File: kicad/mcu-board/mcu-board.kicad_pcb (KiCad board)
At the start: 2 copper layers, 54.5 x 46.3 mm, 64 parts, among them J10 Conn_01x02, J11 Conn_01x02, J12 UJ20-C-H-G-SMT-P16-TR, J13 Conn_01x06, J2 Conn_01x06, J3 Conn_01x01, J4 Conn_01x02, J5 Conn_01x02, J6 Conn_01x02, J7 Conn_01x03, J8 Conn_01x04, J9 Conn_01x02, Q1 Q_NPN_CEB, SW1 SW_Push, SW2 SW_Push, U1 Lora1276-C1-868, U2 ESP32-S3-WROOM-1U-N16R8, U3 LM66200DRLR, U4 AP3445LW6-7

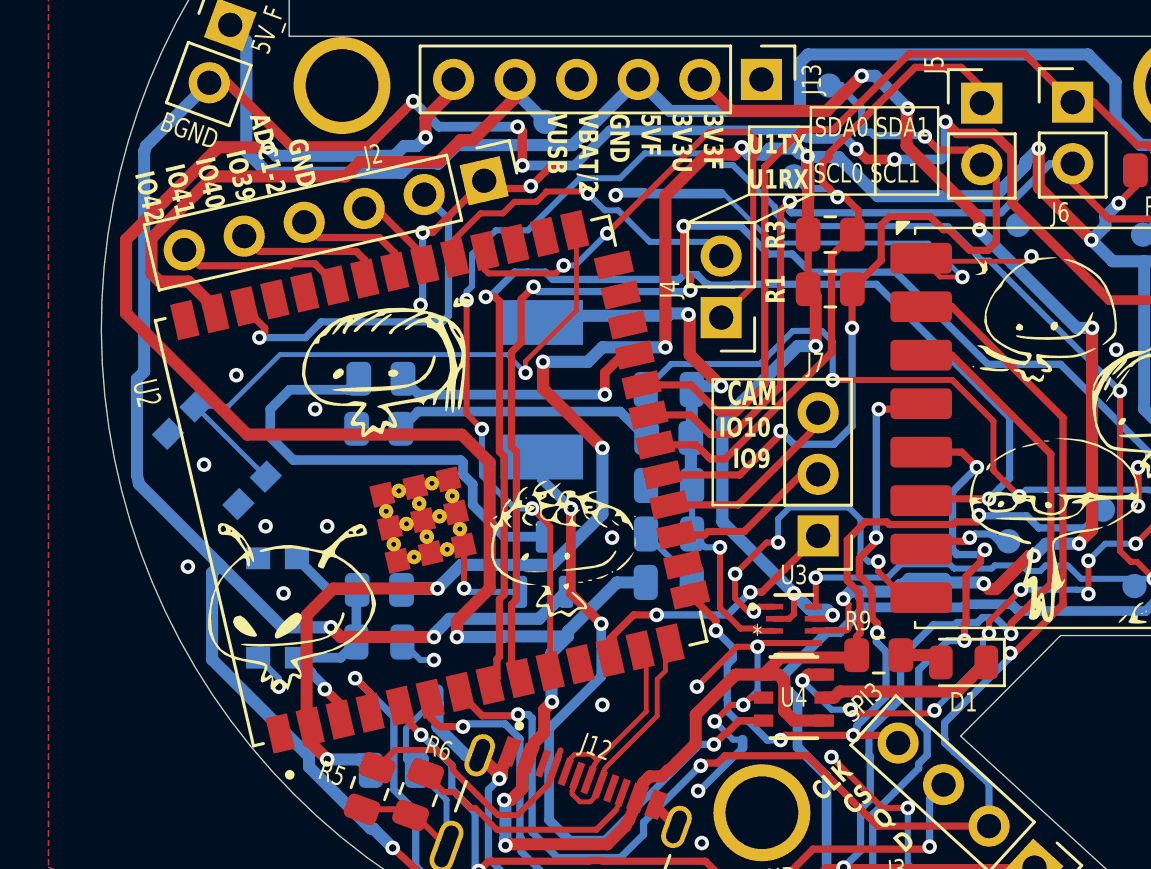
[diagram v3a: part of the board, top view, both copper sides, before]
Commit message: chore: Fixed led footprint from 0805 to 0603, and edited title for buzzer
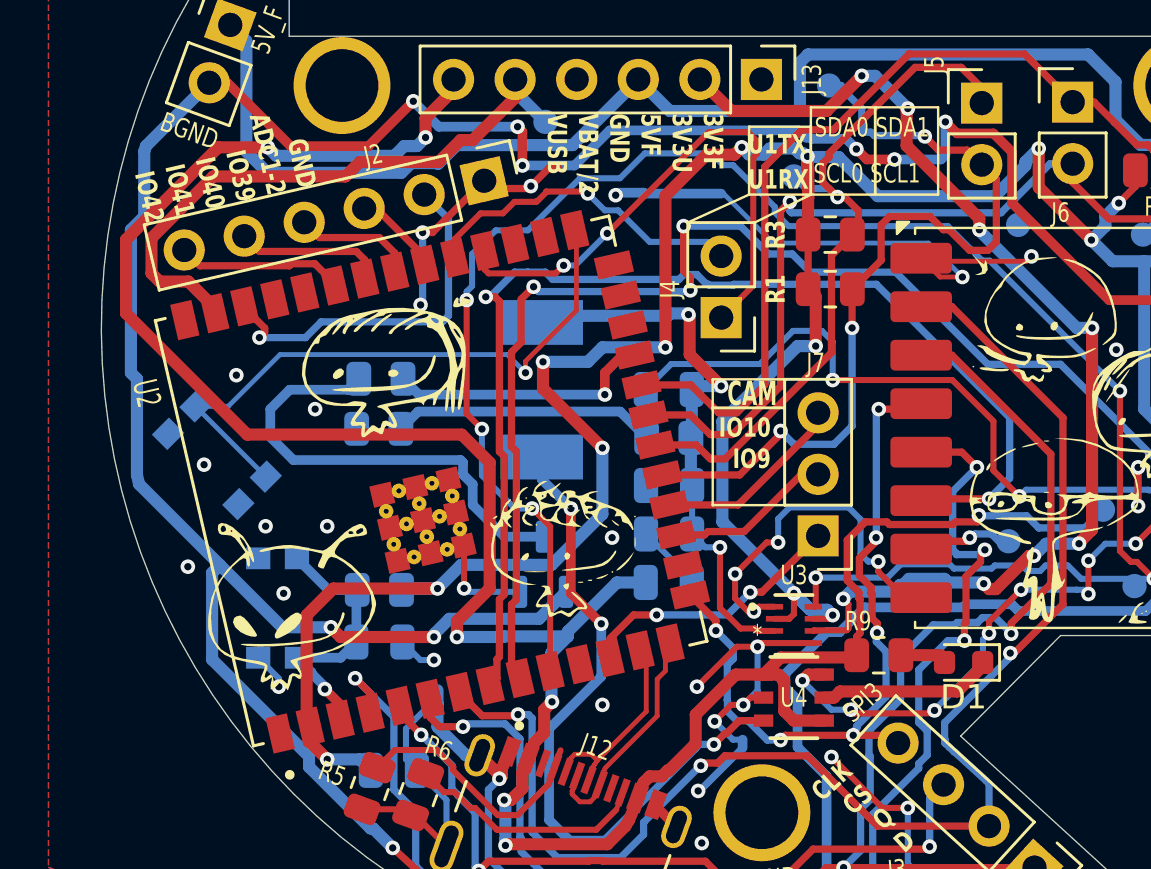
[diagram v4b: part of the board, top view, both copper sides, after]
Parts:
- D1: footprint LED_SMD:LED_0805_2012Metric -> LED_SMD:LED_0603_1608Metric
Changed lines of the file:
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@@
 		(embedded_fonts no)
 	)
-	(footprint "LED_SMD:LED_0805_2012Metric"
+	(footprint "LED_SMD:LED_0603_1608Metric"
 		(layer "F.Cu")
 		(at 113 112.3 180)
-		(descr "LED SMD 0805 (2012 Metric), square (rectangular) end terminal, IPC-7351 nominal, (Body size source: https://docs.google.com/spreadsheets/d/1BsfQQcO9C6DZCsRaXUlFlo91Tg2WpOkGARC1WS5S8t0/edit?usp=sharing), generated with kicad-footprint-generator")
+		(descr "LED SMD 0603 (1608 Metric), square (rectangular) end terminal, IPC-7351 nominal, (Body size source: http://www.tortai-tech.com/upload/download/2011102023233369053.pdf), generated with kicad-footprint-generator")
 		(tags "LED")
 		(property "Reference" "D1"
-			(at 0 -1.65 0)
+			(at 0 -1.43 180)
 			(layer "F.SilkS")
 			(effects
 				(font
-					(size 0.8 0.6)
+					(size 1 1)
 					(thickness 0.15)
 				)
@@
 		)
 		(property "Value" "LED"
-			(at 0 1.65 0)
+			(at 0 1.43 180)
 			(layer "F.Fab")
 			(effects
@@
 		)
 		(property "Datasheet" "~"
-			(at 0 0 0)
+			(at 0 0 180)
 			(layer "F.Fab")
 			(hide yes)
@@
 		)
 		(property "Description" "Light emitting diode"
-			(at 0 0 0)
+			(at 0 0 180)
 			(layer "F.Fab")
 			(hide yes)
@@
 		(attr smd)
 		(fp_line
-			(start 1 -0.96)
-			(end -1.685 -0.96)
+			(start 0.8 -0.735)
+			(end -1.485 -0.735)
 			(stroke
 				(width 0.12)
@@
 		)
 		(fp_line
-			(start -1.685 0.96)
-			(end 1 0.96)
+			(start -1.485 0.735)
+			(end 0.8 0.735)
 			(stroke
 				(width 0.12)
@@
 		)
 		(fp_line
-			(start -1.685 -0.96)
-			(end -1.685 0.96)
+			(start -1.485 -0.735)
+			(end -1.485 0.735)
 			(stroke
 				(width 0.12)
@@
 		)
 		(fp_line
-			(start 1.68 0.95)
-			(end -1.68 0.95)
+			(start 1.48 0.73)
+			(end -1.48 0.73)
 			(stroke
 				(width 0.05)
@@
 		)
 		(fp_line
-			(start 1.68 -0.95)
-			(end 1.68 0.95)
+			(start 1.48 -0.73)
+			(end 1.48 0.73)
 			(stroke
 				(width 0.05)
@@
 		)
 		(fp_line
-			(start -1.68 0.95)
-			(end -1.68 -0.95)
+			(start -1.48 0.73)
+			(end -1.48 -0.73)
 			(stroke
 				(width 0.05)
@@
 		)
 		(fp_line
-			(start -1.68 -0.95)
-			(end 1.68 -0.95)
+			(start -1.48 -0.73)
+			(end 1.48 -0.73)
 			(stroke
 				(width 0.05)
@@
 		)
 		(fp_line
-			(start 1 0.6)
-			(end 1 -0.6)
+			(start 0.8 0.4)
+			(end 0.8 -0.4)
 			(stroke
 				(width 0.1)
@@
 		)
 		(fp_line
-			(start 1 -0.6)
-			(end -0.7 -0.6)
+			(start 0.8 -0.4)
+			(end -0.5 -0.4)
 			(stroke
 				(width 0.1)
@@
 		)
 		(fp_line
-			(start -0.7 -0.6)
-			(end -1 -0.3)
+			(start -0.5 -0.4)
+			(end -0.8 -0.1)
 			(stroke
 				(width 0.1)
@@
 		)
 		(fp_line
-			(start -1 0.6)
-			(end 1 0.6)
+			(start -0.8 0.4)
+			(end 0.8 0.4)
 			(stroke
 				(width 0.1)
@@
 		)
 		(fp_line
-			(start -1 -0.3)
-			(end -1 0.6)
+			(start -0.8 -0.1)
+			(end -0.8 0.4)
 			(stroke
 				(width 0.1)
@@
 		)
 		(fp_text user "${REFERENCE}"
-			(at 0 0 0)
+			(at 0 0 180)
 			(layer "F.Fab")
 			(effects
 				(font
-					(size 0.5 0.5)
-					(thickness 0.08)
+					(size 0.4 0.4)
+					(thickness 0.06)
 				)
 			)
 		)
 		(pad "1" smd roundrect
-			(at -0.9375 0 180)
-			(size 0.975 1.4)
+			(at -0.7875 0 180)
+			(size 0.875 0.95)
 			(layers "F.Cu" "F.Mask" "F.Paste")
 			(roundrect_rratio 0.25)
@@
 		)
 		(pad "2" smd roundrect
-			(at 0.9375 0 180)
-			(size 0.975 1.4)
+			(at 0.7875 0 180)
+			(size 0.875 0.95)
 			(layers "F.Cu" "F.Mask" "F.Paste")
 			(roundrect_rratio 0.25)
@@
 		)
 		(embedded_fonts no)
-		(model "${KICAD9_3DMODEL_DIR}/LED_SMD.3dshapes/LED_0805_2012Metric.stpZ"
+		(model "${KICAD9_3DMODEL_DIR}/LED_SMD.3dshapes/LED_0603_1608Metric.stpZ"
 			(offset
 				(xyz 0 0 0)
@@
 	)
 	(segment
-		(start 78.9 100.600599)
-		(end 79.2 100.300599)
-		(width 0.5)
-		(layer "B.Cu")
-		(net 57)
-	)
-	(segment
 		(start 88.65 119.15)
 		(end 89.45 119.95)
@@
 	)
 	(segment
+		(start 78.9 100.600599)
+		(end 78.65 100.350599)
+		(width 0.5)
+		(layer "B.Cu")
+		(net 57)
+	)
+	(segment
 		(start 85.999 116.611075)
 		(end 88.537925 119.15)
@@
 	)
 	(segment
-		(start 78.986115 104.944365)
-		(end 78.9 104.568454)
-		(width 0.5)
-		(layer "B.Cu")
-		(net 57)
-	)
-	(segment
-		(start 82.320875 108.279125)
-		(end 78.986115 104.944365)
-		(width 0.5)
-		(layer "B.Cu")
-		(net 57)
-	)
-	(segment
 		(start 123.991364 97.35)
 		(end 121.7 97.35)
@@
 	)
 	(segment
-		(start 79.2 91.222341)
-		(end 79.273606 90.994482)
+		(start 95.4875 110.5)
+		(end 91.787925 110.5)
 		(width 0.5)
 		(layer "B.Cu")
@@
 	)
 	(segment
-		(start 95.4875 110.5)
-		(end 91.787925 110.5)
+		(start 79.2 93.9)
+		(end 79.2 91.222341)
 		(width 0.5)
 		(layer "B.Cu")
@@
 	)
 	(segment
-		(start 84.89175 110.85)
-		(end 82.320875 108.279125)
+		(start 78.9 104.568454)
+		(end 78.9 100.600599)
 		(width 0.5)
 		(layer "B.Cu")
@@
 	)
 	(segment
-		(start 91.787925 110.5)
-		(end 91.15 111.137925)
+		(start 78.986115 104.944365)
+		(end 78.9 104.568454)
 		(width 0.5)
 		(layer "B.Cu")
@@
 	)
 	(segment
-		(start 78.9 104.568454)
-		(end 78.9 100.600599)
+		(start 84.89175 110.85)
+		(end 82.320875 108.279125)
 		(width 0.5)
 		(layer "B.Cu")
@@
 	)
 	(segment
-		(start 79.2 100.300599)
-		(end 79.2 91.222341)
+		(start 91.787925 110.5)
+		(end 91.15 111.137925)
+		(width 0.5)
+		(layer "B.Cu")
+		(net 57)
+	)
+	(segment
+		(start 79.2 91.222341)
+		(end 79.273606 90.994482)
 		(width 0.5)
 		(layer "B.Cu")
@@
 	)
 	(segment
+		(start 78.65 94.45)
+		(end 79.2 93.9)
+		(width 0.5)
+		(layer "B.Cu")
+		(net 57)
+	)
+	(segment
+		(start 82.320875 108.279125)
+		(end 78.986115 104.944365)
+		(width 0.5)
+		(layer "B.Cu")
+		(net 57)
+	)
+	(segment
 		(start 86.9 110.85)
 		(end 84.89175 110.85)
@@
 	)
 	(segment
-		(start 106.663571 90.648)
-		(end 106.498 90.648)
-		(width 0.4)
+		(start 78.65 100.350599)
+		(end 78.65 94.45)
+		(width 0.5)
 		(layer "B.Cu")
 		(net 57)
@@
 		(layer "B.Cu")
 		(net 57)
+	)
+	(segment
+		(start 106.663571 90.648)
+		(end 106.498 90.648)
+		(width 0.4)
+		(layer "B.Cu")
+		(net 57)

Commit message: fix: Fixed the mcu-board and preparing for the panelisation
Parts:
- added R12: 5.1k, Resistor_SMD:R_0805_2012Metric, B.Cu at (125.1, 103.5)
- moved TP5 15.9 mm to (130.1, 95.3)
- moved TP4 9.68 mm to (124.8, 98.1)
- moved TP6 8.49 mm to (129.5, 105.7)
- moved TP7 7.71 mm to (129.7, 103.5)
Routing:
- net /LoRa_IRQ: track 56.8 -> 63.9 mm
- net /POWER_ST: track 76.2 -> 82.1 mm
- net +3V3: track 124.4 -> 130.0 mm
- net /DI1: track 3.32 -> 4.54 mm
- net /DI2: track 4.61 -> 5.28 mm
- net GND: vias 45 -> 44
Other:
- board text added: "DI1"
- board text added: "DI2"
- board text added: "DI4 DI3"
- board text removed: "DI1 DI2"
- board text removed: "DI3 DI4"

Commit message: feat: finished pcb, might add more artwork later?
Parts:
- removed the C6 at (100.8, 109.0)
- removed D1: LED, LED_SMD:LED_0603_1608Metric
- removed the G*** at (83.6, 109.0)
- removed the G*** at (121.7, 101.8)
- removed the G*** at (89.4, 100.2)
- removed the G*** at (116.5, 106.5)
- removed the G*** at (96.7, 107.5)
- removed the G*** at (116.5, 98.2)
- removed J10, J11, J9: Conn_01x02, Connector_PinHeader_2.54mm:PinHeader_1x02_P2.54mm_Vertical
- removed J13: Conn_01x06, Connector_PinHeader_2.54mm:PinHeader_1x06_P2.54mm_Vertical
- removed the J6 at (117.5, 89.2)
- removed J8: Conn_01x04, Connector_PinHeader_2.54mm:PinHeader_1x04_P2.54mm_Vertical
- removed L1: 2u2H, PSAT_Library:IND_SPM6530T-1R5M100
- removed the R7 at (100.8, 103.0)
- removed the R8 at (88.9, 102.7)
- removed the R9 at (109.5, 112.0)
- removed the TP15 at (120.4, 94.7)
- added C7: 0.1uf, Capacitor_SMD:C_0805_2012Metric, B.Cu at (84.9, 110.7)
- added C8: 1u, Capacitor_SMD:C_0805_2012Metric, B.Cu at (123.4, 100.1)
- added C9: 1u, Capacitor_SMD:C_0805_2012Metric, B.Cu at (123.4, 102.1)
- added G***: LOGO, LOGO, F.Cu at (95.8, 121.3)
- added G***: LOGO, LOGO, B.Cu at (112.0, 94.2)
- added G***: LOGO, LOGO, F.Cu at (119.2, 102.5)
- added G***: LOGO, LOGO, F.Cu at (113.5, 88.4)
- added G***: LOGO, LOGO, F.Cu at (91.5, 104.8)
- added G***: LOGO, LOGO, B.Cu at (117.0, 89.5)
- added G***: LOGO, LOGO, B.Cu at (110.4, 90.3)
- added G***: LOGO, LOGO, B.Cu at (117.2, 94.9)
- added G***: LOGO, LOGO, B.Cu at (113.3, 89.5)
- added G***: LOGO, LOGO, B.Cu at (114.3, 92.3)
- added J1: Conn_01x03, Connector_PinHeader_2.54mm:PinHeader_1x03_P2.54mm_Vertical, F.Cu at (106.5, 88.3)
- added TP15: TestPoint, TestPoint:TestPoint_Pad_D1.0mm, B.Cu at (121.4, 108.8)
- added TP15: TestPoint, TestPoint:TestPoint_Pad_D1.0mm, B.Cu at (113.6, 107.8)
- added TP17: TestPoint, TestPoint:TestPoint_Pad_D1.0mm, F.Cu at (103.7, 115.0)
- added TP18: TestPoint, TestPoint:TestPoint_Pad_D1.0mm, F.Cu at (104.7, 124.0)
- added TP19: TestPoint, TestPoint:TestPoint_Pad_D1.0mm, F.Cu at (87.4, 117.0)
- added TP20: TestPoint, TestPoint:TestPoint_Pad_D1.0mm, B.Cu at (120.1, 104.0)
- added TP21: TestPoint, TestPoint:TestPoint_Pad_D1.0mm, B.Cu at (127.2, 105.2)
- added TP22: TestPoint, TestPoint:TestPoint_Pad_D1.0mm, B.Cu at (119.0, 109.5)
- added TP23: TestPoint, TestPoint:TestPoint_Pad_D1.0mm, F.Cu at (101.1, 97.0)
- added VBAT1: TestPoint, TestPoint:TestPoint_Pad_D1.0mm, B.Cu at (97.3, 122.8)
- C1: renamed from C7; value 0.1uf -> 1uf
- C3, C4: value 22uF -> 0.1uf; moved to F.Cu
- C5: value 22pF -> 0.1uf
- J2: value Conn_01x06 -> Conn_01x02; footprint Connector_PinHeader_2.54mm:PinHeader_1x06_P2.54mm_Vertical -> Connector_PinHeader_2.54mm:PinHeader_1x02_P2.54mm_Vertical
- J3: value Conn_01x01 -> 533980471; footprint Connector_PinHeader_2.54mm:PinHeader_1x01_P2.54mm_Vertical -> PSAT_Library:MOLEX_533980471
- J4, J5: value Conn_01x02 -> 533980471; footprint Connector_PinHeader_2.54mm:PinHeader_1x02_P2.54mm_Vertical -> PSAT_Library:MOLEX_533980471
- J7: value Conn_01x03 -> 533980471; footprint Connector_PinHeader_2.54mm:PinHeader_1x03_P2.54mm_Vertical -> PSAT_Library:MOLEX_533980471; moved to B.Cu
- Q1: value Q_NPN_CEB -> MMBT619; footprint Package_TO_SOT_SMD:SOT-23-3 -> Package_TO_SOT_SMD:SOT-23; moved to F.Cu
- R1, R2, R3, R4: value 4.7k -> 5.1k; moved to B.Cu
- R5: renamed from R11; value 5.1k -> 10k
- R9: renamed from R10; moved to F.Cu
- SW1: footprint Button_Switch_SMD:SW_Push_1P1T_NO_CK_KMR2 -> Button_Switch_SMD:SW_Tactile_SPST_NO_Straight_CK_PTS636Sx25SMTRLFS; moved to F.Cu
- SW2: footprint Button_Switch_SMD:SW_Push_1P1T_NO_CK_KMR2 -> Button_Switch_SMD:SW_Tactile_SPST_NO_Straight_CK_PTS636Sx25SMTRLFS
- TP11, TP12, TP13: moved to F.Cu
- U2: footprint PSAT_Library:XCVR_ESP32-S3-WROOM-1U-N16R8 -> footprints2:ESP32-S3-WROOM-1U
- U3: footprint footprints:SOT-5X3_DRL_TEX -> footprints2:SOT-5X3_DRL_TEX; moved to B.Cu
- U4: value AP3445LW6-7 -> TLV75733PDBVR; footprint PSAT_Library:SOT26_AP3445_DIO-L -> footprints2:TLV75733PDBVR; moved to B.Cu
- moved TP5 37.1 mm to (93.1, 98.8)
- moved R2 33.0 mm to (89.4, 101.5), turned to -90 degrees
- moved TP6 33.0 mm to (97.0, 100.6)
- moved TP4 32.1 mm to (94.5, 108.8)
- moved TP13 31.8 mm to (129.7, 105.7), turned to 0 degrees
- moved R4 31.7 mm to (94.5, 101.6), turned to 90 degrees
- moved C3 29.4 mm to (129.9, 102.7), turned to -90 degrees
- moved TP14 24.8 mm to (124.2, 108.2)
- moved TP10 23.7 mm to (114.9, 103.8)
- moved C4 22.8 mm to (80.0, 95.8), turned to 180 degrees
- moved TP3 20.8 mm to (91.4, 101.8)
- moved SW1 20.2 mm to (82.2, 90.0), turned to -103 degrees
- moved TP2 19.7 mm to (96.7, 109.6)
- moved U4 18.5 mm to (119.5, 101.2), turned to 90 degrees
- moved C5 17.6 mm to (83.2, 101.5), turned to 90 degrees
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- renumbered C1 to C2, C2 to C6, J12 to J6, R5 to R6, R6 to R7, R12 to R8
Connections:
- C3 pad 1: GND -> +3V3
- C3 pad 2: +3V3_USB -> GND
- C4 pad 1: GND -> /VBAT_IO1
- C4 pad 2: +3V3_USB -> GND
- C5 pad 1: +3V3_USB -> GND
- C5 pad 2: Net-(U4-FB) -> /LIGHT_2_ADC1CH1_IO2
- J2 pad 1: GND -> /IO39
- J2 pad 2: /ADC1_CH2 -> /IO45
- J3 pad 1: GND -> /I2C0_SCL_IO4
- J4 pad 1: /U1RX -> /I2C1_SCL_IO40
- J4 pad 2: /U1TX -> /I2C1_SDA_IO41
- J5 pad 1: /I2CEXT0_SDA -> /CAM_IO13
- J5 pad 2: /I2CEXT0_SCL -> /CAM_IO14
- J7 pad 1: /SERVO_PWM -> /VBAT_IO1
- J7 pad 2: /CAM_GPIO9 -> +3V3_PSU_LDO
- J7 pad 3: /CAM_GPIO10 -> GND
- Q1 pad 1: BUZ_GND -> Net-(Q1-B)
- Q1 pad 3: Net-(Q1-B) -> BUZ_GND
- R1 pad 1: /I2CEXT0_SDA -> /I2C0_SDA_IO5
- R2 pad 1: /I2CEXT1_SDA -> /I2C1_SDA_IO41
- R3 pad 2: /I2CEXT0_SCL -> /I2C0_SCL_IO4
- R4 pad 2: /I2CEXT1_SCL -> /I2C1_SCL_IO40
- R8 pad 1: +3V3 -> +3V3_LDO_LOCAL
- R8 pad 2: /POWER_ST -> /Power Management/POWER_ST
- R9 pad 1: /BUZZER -> /BUZZER_IO38
- TP1 pad 1: GND -> /~{LORA_EN}_IO3
- TP10 pad 1: /V_BAT/2 -> /LORA_SPI3_CS_IO46
- TP11 pad 1: /POWER_ST -> /DI1
- TP12 pad 1: V_USB -> /DI2
- TP13 pad 1: GND -> /DI3
- TP14 pad 1: +5V_FUSED -> /DI4
- TP16 pad 1: /I2CEXT1_SCL -> /LORA_IRQ_IO9
- TP2 pad 1: /I2CEXT0_SDA -> /I2C0_SDA_IO5
- TP3 pad 1: /I2CEXT0_SCL -> /I2C1_SDA_IO41
- TP4 pad 1: /DI1 -> /I2C0_SCL_IO4
- TP5 pad 1: /DI2 -> /I2C1_SCL_IO40
- TP6 pad 1: /DI3 -> /SERVO_IO48
- TP7 pad 1: /DI4 -> /LORA_SPI3_Q_IO12
- TP8 pad 1: /LoRa_IRQ -> /LORA_SPI3_D_IO11
- TP9 pad 1: /DI5 -> /LORA_SPI3_CLK_IO10
- U1 pad 14: /LoRa_IRQ -> /LORA_IRQ_IO9
- U1 pad 2: /SPI3_Q -> /LORA_SPI3_Q_IO12
- U1 pad 3: /SPI3_D -> /LORA_SPI3_D_IO11
- U1 pad 4: /SPI3_CLK -> /LORA_SPI3_CLK_IO10
- U1 pad 5: /SPI3_CS0_O -> /LORA_SPI3_CS_IO46
- U1 pad 6: /~{LoRa_EN} -> /~{LORA_EN}_IO3
- U2 pad 10: /POWER_ST -> unconnected-(U2-IO17-Pad10)
- U2 pad 12: /SERVO_PWM -> unconnected-(U2-IO8-Pad12)
- U2 pad 15: /SPI3_CLK -> /~{LORA_EN}_IO3
- U2 pad 16: unconnected-(U2-IO46-Pad16) -> /LORA_SPI3_CS_IO46
- U2 pad 17: /CAM_GPIO9 -> /LORA_IRQ_IO9
- U2 pad 18: /CAM_GPIO10 -> /LORA_SPI3_CLK_IO10
- U2 pad 19: /I2CEXT0_SCL -> /LORA_SPI3_D_IO11
- U2 pad 20: /I2CEXT0_SDA -> /LORA_SPI3_Q_IO12
- U2 pad 21: /I2CEXT1_SCL -> /CAM_IO13
- U2 pad 22: /I2CEXT1_SDA -> /CAM_IO14
- U2 pad 23: /BUZZER -> /CAM_IO21
- U2 pad 24: unconnected-(U2-IO47-Pad24) -> /CAM_IO47
- U2 pad 25: unconnected-(U2-IO48-Pad25) -> /SERVO_IO48
- U2 pad 26: unconnected-(U2-IO45-Pad26) -> /IO45
- U2 pad 30: /U1RX -> unconnected-(U2-IO37-Pad30)
- U2 pad 31: /U1TX -> /BUZZER_IO38
- U2 pad 32: /GPIO39 -> /IO39
- U2 pad 33: /GPIO40 -> /I2C1_SCL_IO40
- U2 pad 34: /GPIO41 -> /I2C1_SDA_IO41
- U2 pad 35: /GPIO42 -> /LIGHT_1_IO42
- U2 pad 38: /ADC1_CH2 -> /LIGHT_2_ADC1CH1_IO2
- U2 pad 39: /V_BAT/2 -> /VBAT_IO1
- U2 pad 4: /SPI3_CS0_O -> /I2C0_SCL_IO4
- U2 pad 5: /SPI3_CS1_O -> /I2C0_SDA_IO5
- U2 pad 6: /SPI3_D -> /GPS_U1TX_IO6
- U2 pad 7: /SPI3_Q -> /GPS_U1RX_IO7
- U2 pad 8: /~{LoRa_EN} -> unconnected-(U2-IO15-Pad8)
- U2 pad 9: /LoRa_IRQ -> unconnected-(U2-IO16-Pad9)
- U3 pad 3: +3V3_USB -> +3V3_LDO_LOCAL
- U3 pad 6: +3V3_PSU_UNFUSED -> +3V3_PSU_LDO
- U3 pad 8: /POWER_ST -> /Power Management/POWER_ST
- U4 pad 3: Net-(U4-LX) -> V_USB
- U4 pad 4: V_USB -> unconnected-(U4-NC-Pad4)
- U4 pad 5: Net-(D1-K) -> +3V3_LDO_LOCAL
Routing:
- net BUZ_GND: track 128.3 -> 10.8 mm, vias 10 -> 0
- net +5V_FUSED: track 117.1 -> 0.00 mm, vias 2 -> 0
- net GND: track 122.7 -> 15.4 mm, vias 44 -> 35
- net /POWER_ST: track 82.1 -> 0.00 mm, vias 6 -> 0
- net /LoRa_IRQ: track 63.9 -> 0.00 mm, vias 4 -> 0
- net Net-(U4-FB): track 62.7 -> 0.00 mm, vias 11 -> 0
- net /SPI3_D: track 62.5 -> 0.00 mm, vias 4 -> 0
- net /VBAT_IO1: track 0.00 -> 61.0 mm, vias 0 -> 1
- net /SPI3_Q: track 58.2 -> 0.00 mm, vias 3 -> 0
- net /SPI3_CS0_O: track 55.7 -> 0.00 mm, vias 4 -> 0
- net /I2C0_SCL_IO4: track 0.00 -> 49.6 mm, vias 0 -> 2
- net /~{LoRa_EN}: track 48.0 -> 0.00 mm, vias 2 -> 0
- net V_USB: track 100.9 -> 54.6 mm, vias 7 -> 2
- net +3V3_PSU_UNFUSED: track 45.8 -> 0.00 mm, vias 8 -> 0
- net +3V3: track 130.0 -> 84.3 mm, vias 15 -> 3
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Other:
- board text added: "3V3"
- board text added: "3V3_LDO"
- board text added: "3V3_PSU"
- board text added: "CS"
- board text added: "Camera pls"
- board text added: "DI3"
- board text added: "DI4"
- board text added: "Daniel still gotta eat the 2x buldak"
- board text added: "Dedicated to: mr long schlong"
- board text added: "I2C0 + GPS pls"
- board text added: "I2C0_SCL"
- board text added: "I2C0_SDA"
- board text added: "I2C1 + Light pls"
- board text added: "I2C1_SCL"
- board text added: "I2C1_SDA"
- board text added: "IO48"
- board text added: "MCU-BOARD REV 2"
- board text added: "Mr Dan Velasco:"
- board text added: "PST"
- board text added: "Power here pls"
- board text added: "RX_IRQ"
- board text added: "SCLK"
- board text added: "SPID"
- board text added: "SPIQ"
- board text added: "VBAT"
- board text added: "VUSB"
- board text added: "desinged by aids"
- board text added: "~{EN}"
- board text removed: "3V3F 3V3U 5VF GND VBAT/2 VUSB"
- board text removed: "5VF"
- board text removed: "5V_F"
- board text removed: "BOOT"
- board text removed: "BUZ_GND"
- board text removed: "CAM"
- board text removed: "CLK CS Q D"
- board text removed: "DI4 DI3"
- board text removed: "Designed by: aids (might be cooked)"
- board text removed: "EN"
- board text removed: "GND ADC1-2 IO39 IO40 IO41 IO42"
- board text removed: "IO10 IO9"
- board text removed: "LoRa_IRQ"
- board text removed: "MCU-BOARD REV 1"
- board text removed: "POWER_ST"
- board text removed: "SCL0"
- board text removed: "SCL0 SCL1"
- board text removed: "SCL1"
- board text removed: "SDA0"
- board text removed: "SDA0 SDA1"
- board text removed: "SDA1"
- board text removed: "SPI3"
- board text removed: "U1RX"
- board text removed: "U1TX"
- board text removed: "VBAT/2"
- board text removed: "V_USB"
- board text removed: "{dblquote}I apologise Miguel{dblquote}"
